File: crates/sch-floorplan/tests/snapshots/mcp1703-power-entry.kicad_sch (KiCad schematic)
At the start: 8 parts, among them U1 MCP1703Ax-330xxTT

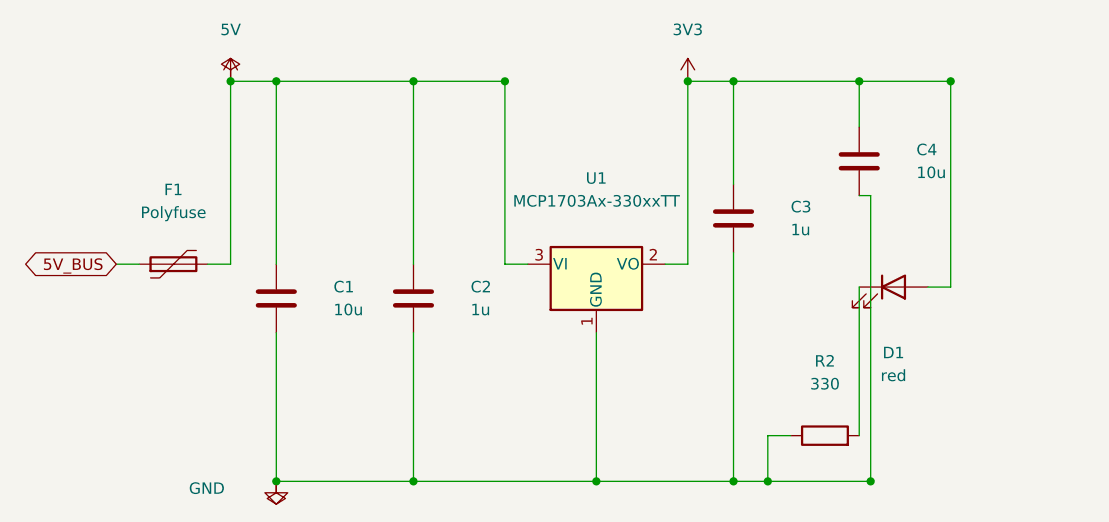
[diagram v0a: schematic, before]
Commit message: sch-doc: pick the smallest standard page from an A5-first ladder
A four-part circuit on A4 is a drawing stranded in one corner of an
empty sheet; the critic scored that a point worse than the snug custom
page it replaced. Starting the ladder at A5 keeps the frame close to
the content while every sheet still lands on a size KiCad and a printer
recognise.

Re-blessed the five snapshots whose critic score held at or above their
pre-change score. grid-demo is left at its baseline: it renders 7 where
it used to render 9.

Claude-Session: https://claude.ai/code/session_01GyGRY43X8yBh8WS1tjEmFz
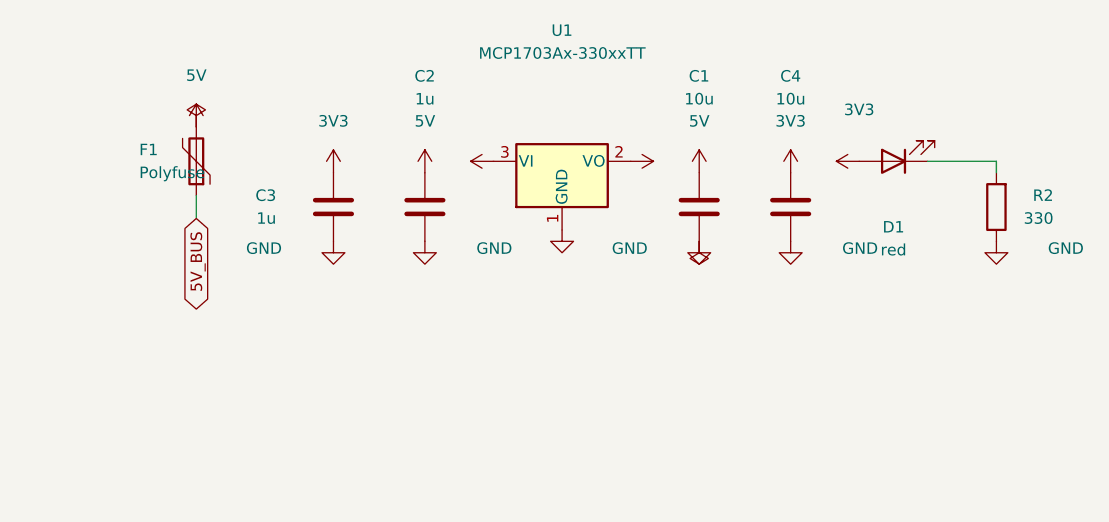
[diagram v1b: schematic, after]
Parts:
- C1, C2, C3, C4, D1, F1, R2, U1: ap_block (none) -> power_entry
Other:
- moved on the sheet: C1, C2, C3, C4, D1, F1, R2, U1
